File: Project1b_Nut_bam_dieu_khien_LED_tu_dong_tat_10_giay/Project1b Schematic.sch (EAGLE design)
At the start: 8 parts, among them U1 ARDUINOR3-BPLACE

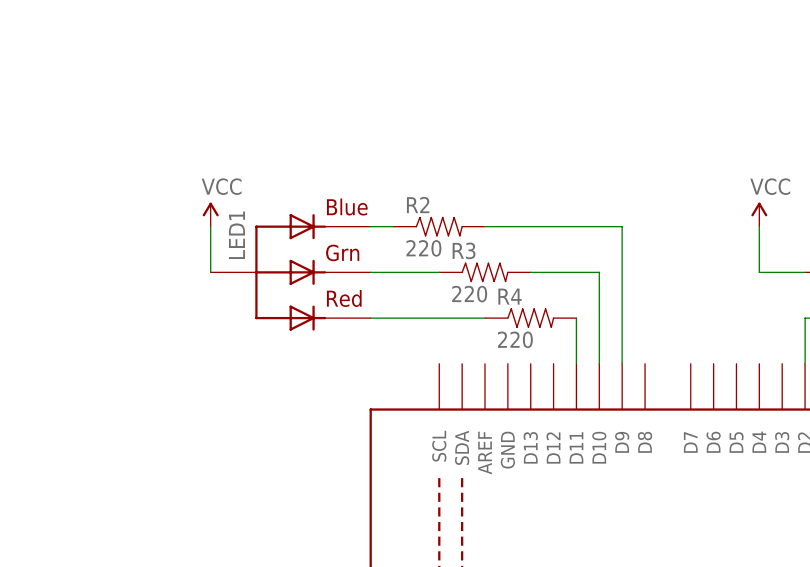
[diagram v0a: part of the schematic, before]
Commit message: Update schematic, breadboard cho nhieu projects.
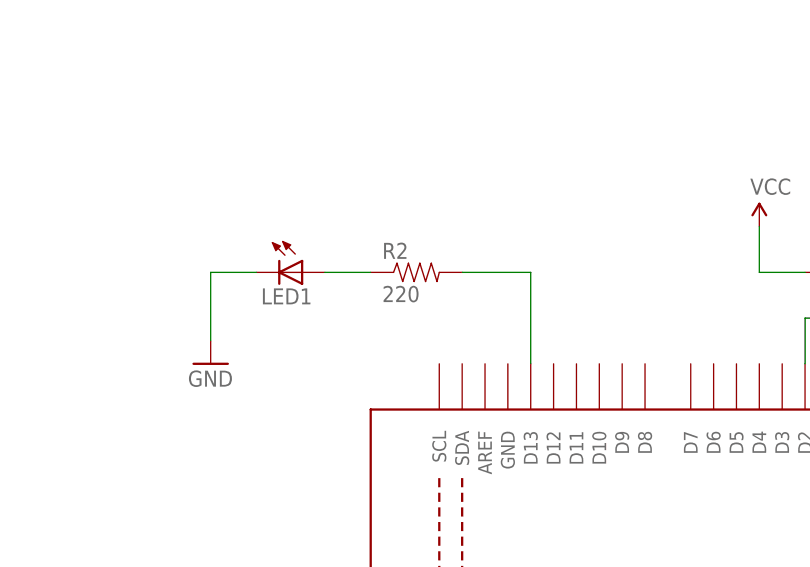
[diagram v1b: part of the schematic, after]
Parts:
- removed R3, R4: 220, SparkFun-Passives:RESISTOR0402-RES
- LED1: value RGBLED_CA-5MM -> (none); device adafruit:RGBLED_CA-5MM -> adafruit:LED
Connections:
- removed net N$3: R2.2, U1.D9
- removed net N$4: LED1.BLUE, R2.1
- removed net N$6: LED1.GREEN, R3.1
- removed net N$7: LED1.RED, R4.1
- net GND: now also LED1.C
- net N$1: now also R2.2, U1.D13; no longer R4.2, U1.D11
- net N$2: now also LED1.A, R2.1; no longer R3.2, U1.D10
- net VCC: no longer LED1.VCC
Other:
- moved on the sheet: R2
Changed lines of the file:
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@@
 <part name="R2" library="SparkFun-Passives" deviceset="RESISTOR" device="0402-RES" value="220"/>
 <part name="S1" library="adafruit" deviceset="40-XX" device=""/>
+<part name="LED1" library="adafruit" deviceset="LED" device=""/>
+<part name="GND2" library="SparkFun-Aesthetics" deviceset="GND" device=""/>
 <part name="GND3" library="SparkFun-Aesthetics" deviceset="GND" device=""/>
 <part name="SUPPLY2" library="SparkFun-Aesthetics" deviceset="VCC" device=""/>
 <part name="FRAME1" library="SparkFun-Aesthetics" deviceset="FRAME-LETTER" device=""/>
-<part name="LED1" library="adafruit" deviceset="RGBLED_CA" device="-5MM"/>
-<part name="R3" library="SparkFun-Passives" deviceset="RESISTOR" device="0402-RES" value="220"/>
-<part name="R4" library="SparkFun-Passives" deviceset="RESISTOR" device="0402-RES" value="220"/>
-<part name="SUPPLY5" library="SparkFun-Aesthetics" deviceset="VCC" device=""/>
 </parts>
 <sheets>
@@
 <instance part="GND1" gate="1" x="81.28" y="40.64"/>
 <instance part="R1" gate="G$1" x="99.06" y="119.38"/>
-<instance part="R2" gate="G$1" x="53.34" y="124.46"/>
+<instance part="R2" gate="G$1" x="50.8" y="119.38"/>
 <instance part="S1" gate="1" x="114.3" y="121.92" rot="MR270"/>
+<instance part="LED1" gate="G$1" x="38.1" y="119.38" rot="R270"/>
+<instance part="GND2" gate="1" x="27.94" y="109.22"/>
 <instance part="GND3" gate="1" x="124.46" y="114.3"/>
 <instance part="SUPPLY2" gate="G$1" x="88.9" y="124.46"/>
 <instance part="FRAME1" gate="G$1" x="-33.02" y="-15.24"/>
 <instance part="FRAME1" gate="V" x="114.3" y="-15.24"/>
-<instance part="LED1" gate="G$1" x="38.1" y="119.38"/>
-<instance part="R3" gate="G$1" x="58.42" y="119.38"/>
-<instance part="R4" gate="G$1" x="63.5" y="114.3"/>
-<instance part="SUPPLY5" gate="G$1" x="27.94" y="124.46"/>
 </instances>
 <busses>
@@
 <wire x1="88.9" y1="119.38" x2="93.98" y2="119.38" width="0.1524" layer="91"/>
 </segment>
-<segment>
-<pinref part="SUPPLY5" gate="G$1" pin="VCC"/>
-<wire x1="27.94" y1="124.46" x2="27.94" y2="119.38" width="0.1524" layer="91"/>
-<pinref part="LED1" gate="G$1" pin="VCC"/>
-</segment>
 </net>
 <net name="GND" class="0">
@@
 </segment>
 <segment>
+<pinref part="LED1" gate="G$1" pin="C"/>
+<wire x1="33.02" y1="119.38" x2="27.94" y2="119.38" width="0.1524" layer="91"/>
+<pinref part="GND2" gate="1" pin="GND"/>
+<wire x1="27.94" y1="119.38" x2="27.94" y2="111.76" width="0.1524" layer="91"/>
+</segment>
+<segment>
 <pinref part="S1" gate="1" pin="P1"/>
 <pinref part="GND3" gate="1" pin="GND"/>
 <wire x1="119.38" y1="119.38" x2="124.46" y2="119.38" width="0.1524" layer="91"/>
 <wire x1="124.46" y1="119.38" x2="124.46" y2="116.84" width="0.1524" layer="91"/>
+</segment>
+</net>
+<net name="N$1" class="0">
+<segment>
+<pinref part="R2" gate="G$1" pin="2"/>
+<pinref part="U1" gate="G$1" pin="D13"/>
+<wire x1="55.88" y1="119.38" x2="63.5" y2="119.38" width="0.1524" layer="91"/>
+<wire x1="63.5" y1="119.38" x2="63.5" y2="109.22" width="0.1524" layer="91"/>
+</segment>
+</net>
+<net name="N$2" class="0">
+<segment>
+<pinref part="R2" gate="G$1" pin="1"/>
+<pinref part="LED1" gate="G$1" pin="A"/>
+<wire x1="45.72" y1="119.38" x2="40.64" y2="119.38" width="0.1524" layer="91"/>
 </segment>
 </net>
@@
 </segment>
 </net>
-<net name="N$1" class="0">
-<segment>
-<pinref part="U1" gate="G$1" pin="D11"/>
-<wire x1="68.58" y1="114.3" x2="68.58" y2="109.22" width="0.1524" layer="91"/>
-<pinref part="R4" gate="G$1" pin="2"/>
-</segment>
-</net>
-<net name="N$2" class="0">
-<segment>
-<pinref part="U1" gate="G$1" pin="D10"/>
-<wire x1="71.12" y1="119.38" x2="71.12" y2="109.22" width="0.1524" layer="91"/>
-<pinref part="R3" gate="G$1" pin="2"/>
-<wire x1="71.12" y1="119.38" x2="63.5" y2="119.38" width="0.1524" layer="91"/>
-</segment>
-</net>
-<net name="N$3" class="0">
-<segment>
-<pinref part="U1" gate="G$1" pin="D9"/>
-<wire x1="73.66" y1="124.46" x2="73.66" y2="109.22" width="0.1524" layer="91"/>
-<pinref part="R2" gate="G$1" pin="2"/>
-<wire x1="58.42" y1="124.46" x2="73.66" y2="124.46" width="0.1524" layer="91"/>
-</segment>
-</net>
-<net name="N$4" class="0">
-<segment>
-<pinref part="LED1" gate="G$1" pin="BLUE"/>
-<pinref part="R2" gate="G$1" pin="1"/>
-<wire x1="45.72" y1="124.46" x2="48.26" y2="124.46" width="0.1524" layer="91"/>
-</segment>
-</net>
-<net name="N$6" class="0">
-<segment>
-<pinref part="LED1" gate="G$1" pin="GREEN"/>
-<pinref part="R3" gate="G$1" pin="1"/>
-<wire x1="45.72" y1="119.38" x2="53.34" y2="119.38" width="0.1524" layer="91"/>
-</segment>
-</net>
-<net name="N$7" class="0">
-<segment>
-<pinref part="R4" gate="G$1" pin="1"/>
-<pinref part="LED1" gate="G$1" pin="RED"/>
-<wire x1="58.42" y1="114.3" x2="45.72" y2="114.3" width="0.1524" layer="91"/>
-</segment>
-</net>
